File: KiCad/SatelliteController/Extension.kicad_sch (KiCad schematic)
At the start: 3 parts, among them J7 CONN_STATUS_PANEL, J8 CONN_PANEL_BAORD_2, J9 CONN_PANEL_BAORD_1

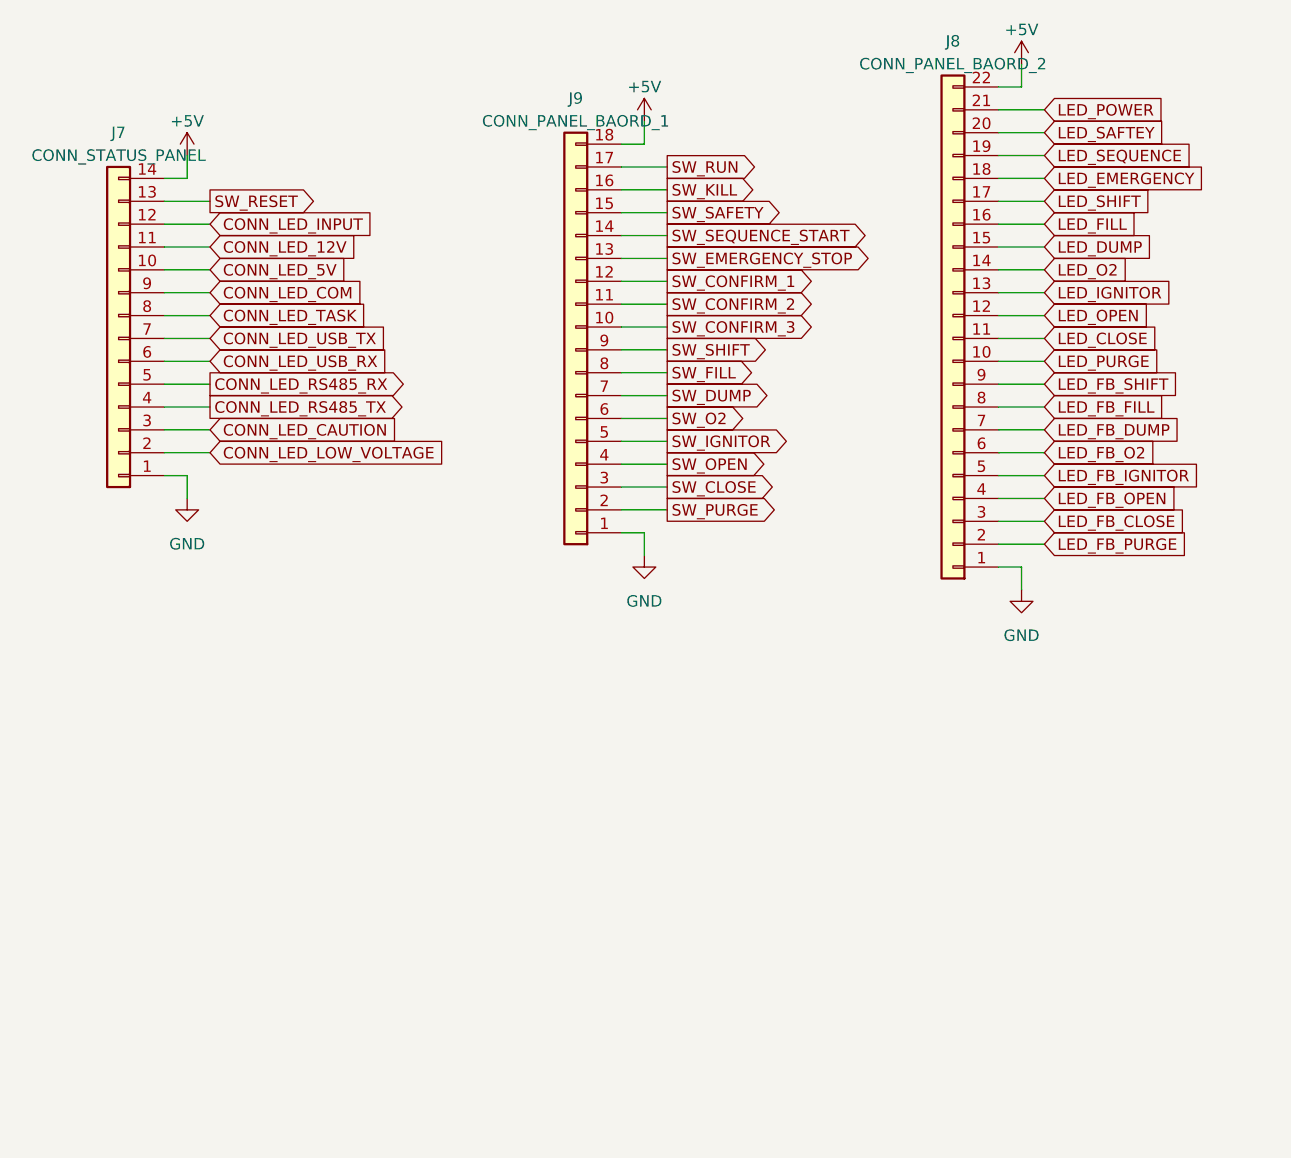
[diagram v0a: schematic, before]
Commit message: 圧力センサとの接続部を追加
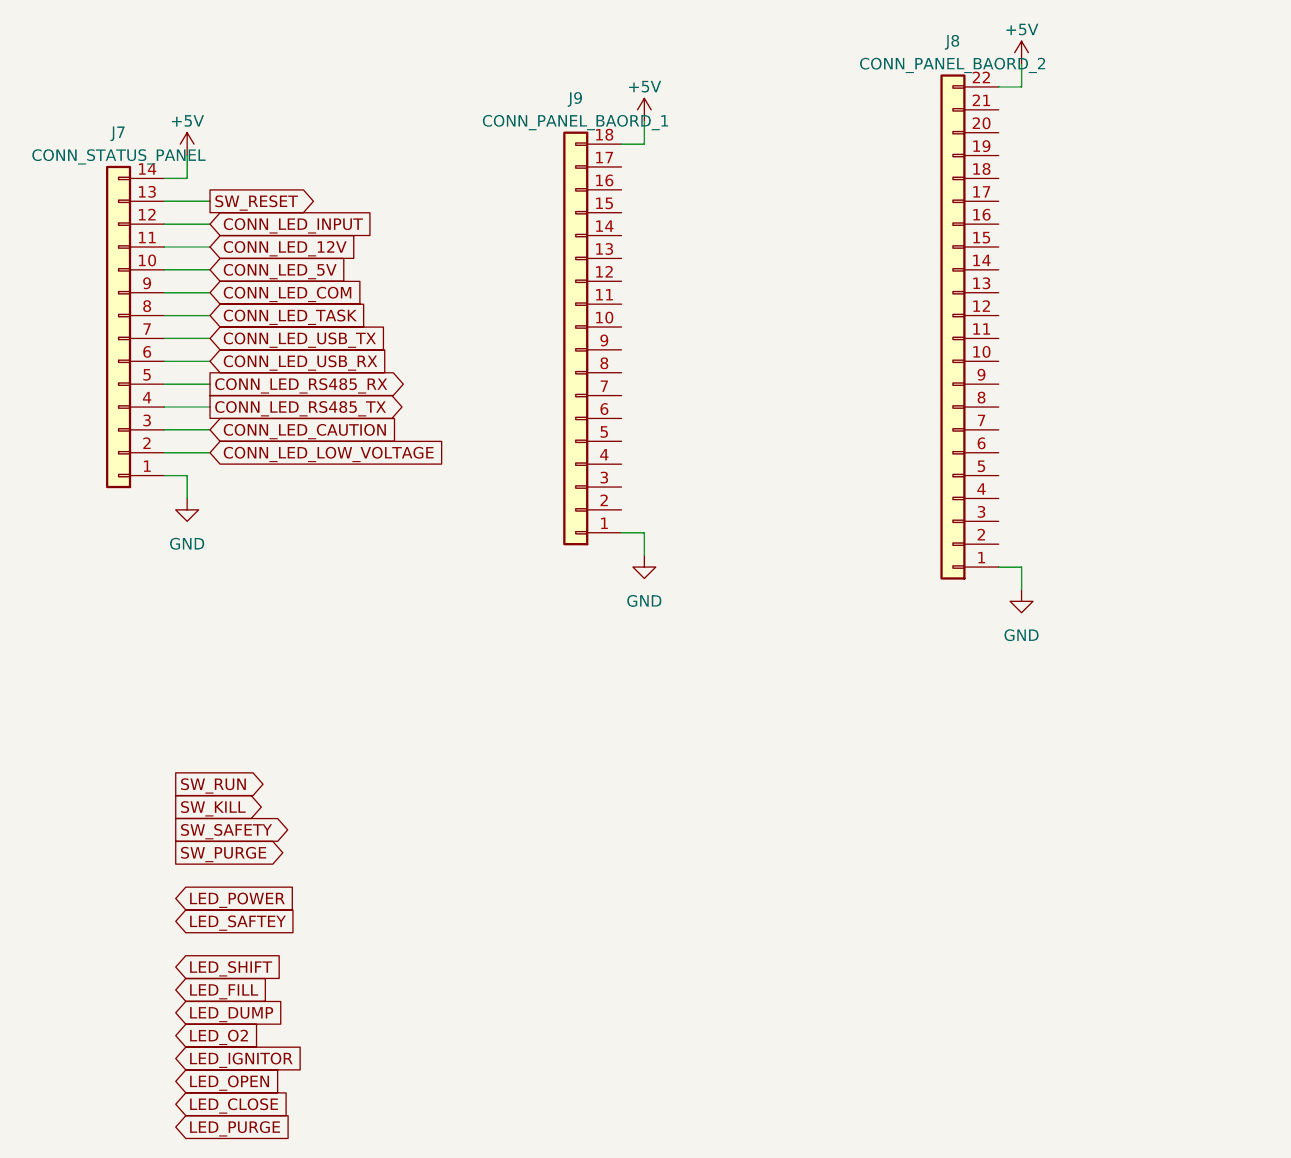
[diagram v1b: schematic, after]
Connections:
- net LED_CLOSE: no longer J8.11 (Pin_11)
- net LED_DUMP: no longer J8.15 (Pin_15)
- net LED_FILL: no longer J8.16 (Pin_16)
- net LED_IGNITOR: no longer J8.13 (Pin_13)
- net LED_O2: no longer J8.14 (Pin_14)
- net LED_OPEN: no longer J8.12 (Pin_12)
- net LED_POWER: no longer J8.21 (Pin_21)
- net LED_PURGE: no longer J8.10 (Pin_10)
- net LED_SAFTEY: no longer J8.20 (Pin_20)
- net LED_SHIFT: no longer J8.17 (Pin_17)
- net SW_KILL: no longer J9.16 (Pin_16)
- net SW_PURGE: no longer J9.2 (Pin_2)
- net SW_RUN: no longer J9.17 (Pin_17)
- net SW_SAFETY: no longer J9.15 (Pin_15)
- net LED_EMERGENCY: no longer names the net of J8.18 (Pin_18)
- net LED_FB_CLOSE: no longer names the net of J8.3 (Pin_3)
- net LED_FB_DUMP: no longer names the net of J8.7 (Pin_7)
- net LED_FB_FILL: no longer names the net of J8.8 (Pin_8)
- net LED_FB_IGNITOR: no longer names the net of J8.5 (Pin_5)
- net LED_FB_O2: no longer names the net of J8.6 (Pin_6)
- net LED_FB_OPEN: no longer names the net of J8.4 (Pin_4)
- net LED_FB_PURGE: no longer names the net of J8.2 (Pin_2)
- net LED_FB_SHIFT: no longer names the net of J8.9 (Pin_9)
- net LED_SEQUENCE: no longer names the net of J8.19 (Pin_19)
- net SW_CLOSE: no longer names the net of J9.3 (Pin_3)
- net SW_CONFIRM_1: no longer names the net of J9.12 (Pin_12)
- net SW_CONFIRM_2: no longer names the net of J9.11 (Pin_11)
- net SW_CONFIRM_3: no longer names the net of J9.10 (Pin_10)
- net SW_DUMP: no longer names the net of J9.7 (Pin_7)
- net SW_EMERGENCY_STOP: no longer names the net of J9.13 (Pin_13)
- net SW_FILL: no longer names the net of J9.8 (Pin_8)
- net SW_IGNITOR: no longer names the net of J9.5 (Pin_5)
- net SW_O2: no longer names the net of J9.6 (Pin_6)
- net SW_OPEN: no longer names the net of J9.4 (Pin_4)
- net SW_SEQUENCE_START: no longer names the net of J9.14 (Pin_14)
- net SW_SHIFT: no longer names the net of J9.9 (Pin_9)

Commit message: ランコンのKiCadプロジェクトをコピーしてサテコンを作成
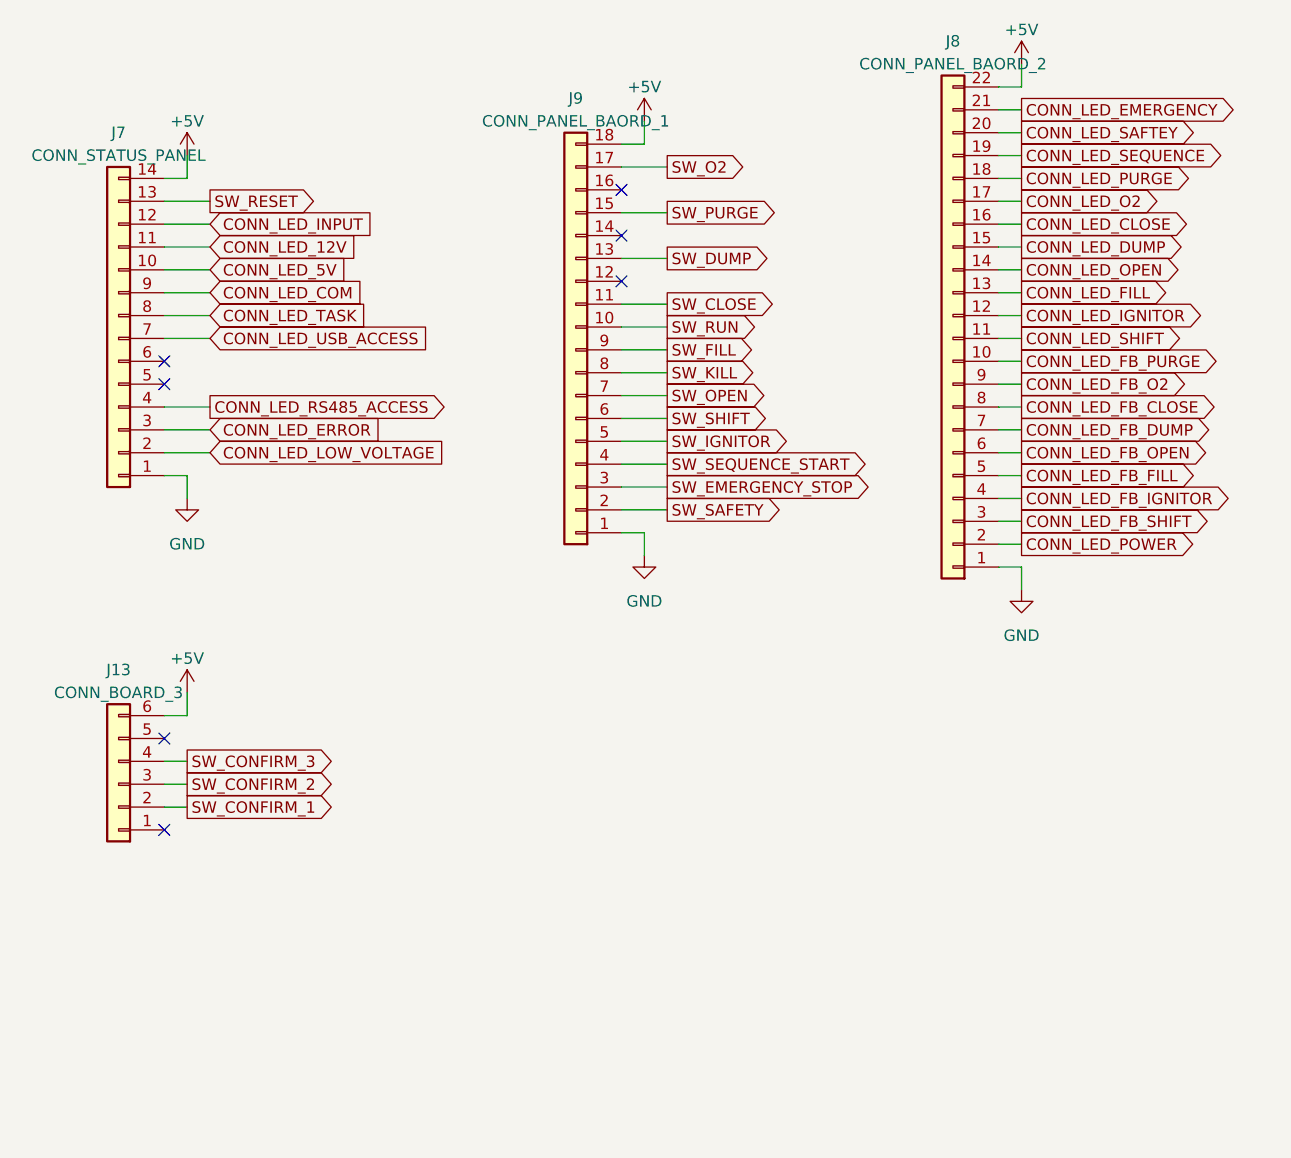
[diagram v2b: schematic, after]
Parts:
- added J13: CONN_BOARD_3, TSRP_Connector_Hirose:DF51A-6DP-2DSA, symbol Connector_Generic:Conn_01x06
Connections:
- net +5V: now also J13.6 (Pin_6)
- net SW_KILL: now also J9.8 (Pin_8)
- net SW_PURGE: now also J9.15 (Pin_15)
- net SW_RUN: now also J9.10 (Pin_10)
- net SW_SAFETY: now also J9.2 (Pin_2)
- net CONN_LED_FB_PURGE: now reaches J8.10 (Pin_10)
- net CONN_LED_SHIFT: now reaches J8.11 (Pin_11)
- net CONN_LED_IGNITOR: now reaches J8.12 (Pin_12)
- net CONN_LED_FILL: now reaches J8.13 (Pin_13)
- net CONN_LED_OPEN: now reaches J8.14 (Pin_14)
- net CONN_LED_DUMP: now reaches J8.15 (Pin_15)
- net CONN_LED_CLOSE: now reaches J8.16 (Pin_16)
- net CONN_LED_O2: now reaches J8.17 (Pin_17)
- net CONN_LED_PURGE: now reaches J8.18 (Pin_18)
- net CONN_LED_SEQUENCE: now reaches J8.19 (Pin_19)
- net CONN_LED_POWER: now reaches J8.2 (Pin_2)
- net CONN_LED_SAFTEY: now reaches J8.20 (Pin_20)
- net CONN_LED_EMERGENCY: now reaches J8.21 (Pin_21)
- net CONN_LED_FB_SHIFT: now reaches J8.3 (Pin_3)
- net CONN_LED_FB_IGNITOR: now reaches J8.4 (Pin_4)
- net CONN_LED_FB_FILL: now reaches J8.5 (Pin_5)
- net CONN_LED_FB_OPEN: now reaches J8.6 (Pin_6)
- net CONN_LED_FB_DUMP: now reaches J8.7 (Pin_7)
- net CONN_LED_FB_CLOSE: now reaches J8.8 (Pin_8)
- net CONN_LED_FB_O2: now reaches J8.9 (Pin_9)
- net SW_CLOSE: now reaches J9.11 (Pin_11)
- net SW_DUMP: now reaches J9.13 (Pin_13)
- net SW_O2: now reaches J9.17 (Pin_17)
- net SW_EMERGENCY_STOP: now reaches J9.3 (Pin_3)
- net SW_SEQUENCE_START: now reaches J9.4 (Pin_4)
- net SW_IGNITOR: now reaches J9.5 (Pin_5)
- net SW_SHIFT: now reaches J9.6 (Pin_6)
- net SW_OPEN: now reaches J9.7 (Pin_7)
- net SW_FILL: now reaches J9.9 (Pin_9)
- net CONN_LED_CAUTION renamed CONN_LED_ERROR
- net CONN_LED_RS485_RX: no longer names the net of J7.5 (Pin_5)
- net CONN_LED_RS485_TX renamed CONN_LED_RS485_ACCESS
- net CONN_LED_USB_RX: no longer names the net of J7.6 (Pin_6)
- net CONN_LED_USB_TX renamed CONN_LED_USB_ACCESS
- new net SW_CONFIRM_1: J13.2 (Pin_2)
- new net SW_CONFIRM_2: J13.3 (Pin_3)
- new net SW_CONFIRM_3: J13.4 (Pin_4)
- no-connect marks 0 -> 7

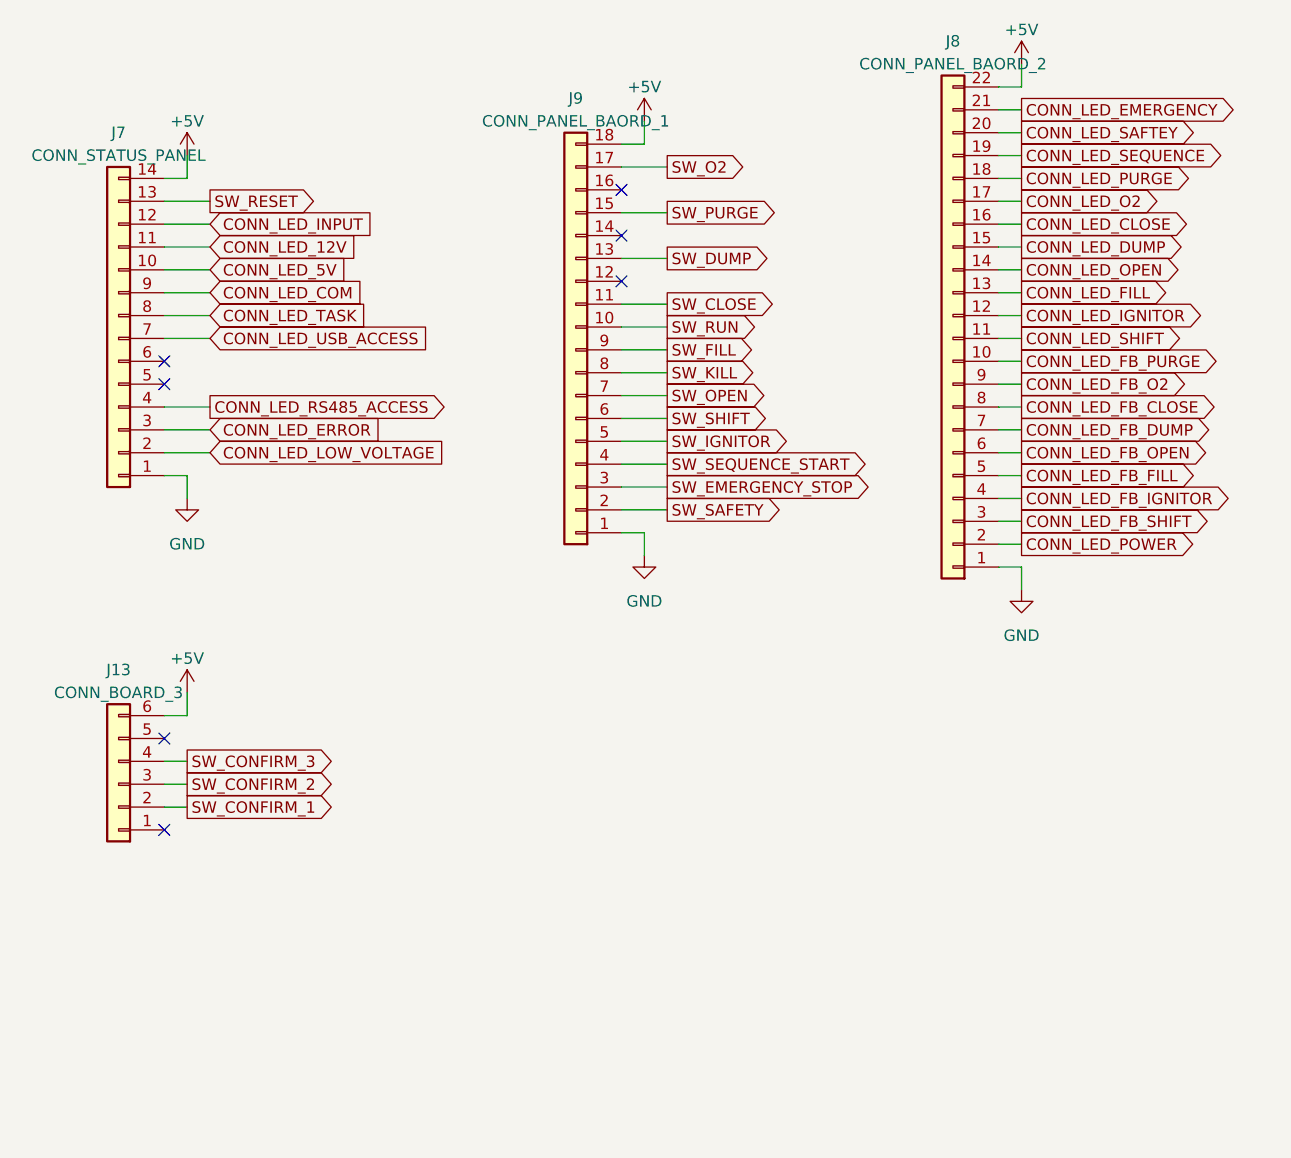
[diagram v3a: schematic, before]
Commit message: 手動操作を削除
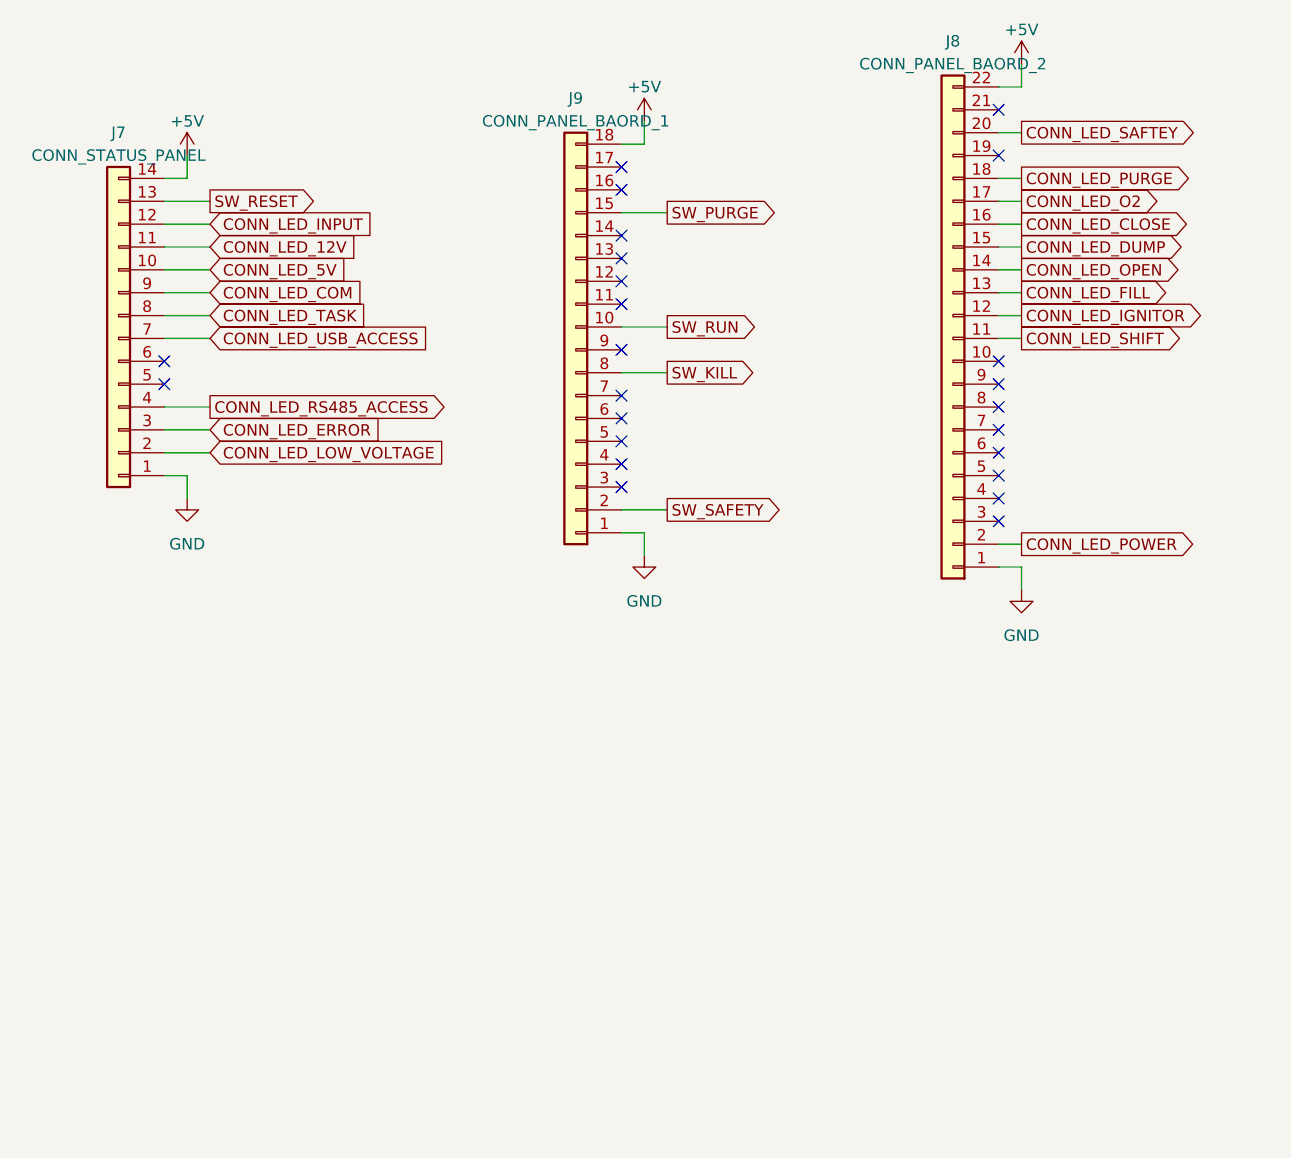
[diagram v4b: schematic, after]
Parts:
- removed J13: CONN_BOARD_3, TSRP_Connector_Hirose:DF51A-6DP-2DSA, symbol Connector_Generic:Conn_01x06
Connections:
- net CONN_LED_EMERGENCY: no longer names the net of J8.21 (Pin_21)
- net CONN_LED_FB_CLOSE: no longer names the net of J8.8 (Pin_8)
- net CONN_LED_FB_DUMP: no longer names the net of J8.7 (Pin_7)
- net CONN_LED_FB_FILL: no longer names the net of J8.5 (Pin_5)
- net CONN_LED_FB_IGNITOR: no longer names the net of J8.4 (Pin_4)
- net CONN_LED_FB_O2: no longer names the net of J8.9 (Pin_9)
- net CONN_LED_FB_OPEN: no longer names the net of J8.6 (Pin_6)
- net CONN_LED_FB_PURGE: no longer names the net of J8.10 (Pin_10)
- net CONN_LED_FB_SHIFT: no longer names the net of J8.3 (Pin_3)
- net CONN_LED_SEQUENCE: no longer names the net of J8.19 (Pin_19)
- net SW_CLOSE: no longer names the net of J9.11 (Pin_11)
- net SW_DUMP: no longer names the net of J9.13 (Pin_13)
- net SW_EMERGENCY_STOP: no longer names the net of J9.3 (Pin_3)
- net SW_FILL: no longer names the net of J9.9 (Pin_9)
- net SW_IGNITOR: no longer names the net of J9.5 (Pin_5)
- net SW_O2: no longer names the net of J9.17 (Pin_17)
- net SW_OPEN: no longer names the net of J9.7 (Pin_7)
- net SW_SEQUENCE_START: no longer names the net of J9.4 (Pin_4)
- net SW_SHIFT: no longer names the net of J9.6 (Pin_6)
- no-connect marks 7 -> 24
